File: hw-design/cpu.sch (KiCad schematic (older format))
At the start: 15 parts, among them P1 CONN_02X05, P2 CONN_02X05, U4 LPC1113FBD48/302, X1 10MHz

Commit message: replacing some cached symbols by kicad-library symbols
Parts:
- X1: symbol CRYSTAL -> Crystal
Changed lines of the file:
@@
 $EndComp
 $Comp
-L CRYSTAL X1
+L Crystal X1
 U 1 1 548B6D9D
 P 2700 4700
@@
 	8750 4850 8650 4850
 Wire Wire Line
-	7950 4850 7950 5250
+	7950 4850 7950 4950
+Wire Wire Line
+	7950 4950 7950 5050
+Wire Wire Line
+	7950 5050 7950 5150
+Wire Wire Line
+	7950 5150 7950 5250
 Connection ~ 7950 5050
 Connection ~ 7950 4950
@@
 	5650 3700 5850 3700
 Wire Wire Line
-	3000 4700 3250 4700
+	2850 4700 3100 4700
+Wire Wire Line
+	3100 4700 3250 4700
 Wire Wire Line
 	3100 4850 3100 4700
 Connection ~ 3100 4700
 Wire Wire Line
-	2250 4500 2250 4850
+	2250 4500 2250 4700
+Wire Wire Line
+	2250 4700 2250 4850
 Wire Wire Line
 	2250 4500 3250 4500
 Wire Wire Line
-	2400 4700 2250 4700
+	2550 4700 2250 4700
 Connection ~ 2250 4700
 Wire Wire Line
 	4350 4950 4350 5050
 Wire Wire Line
-	4350 5050 4550 5050
+	4350 5050 4450 5050
+Wire Wire Line
+	4450 5050 4550 5050
 Wire Wire Line
 	4550 5050 4550 4950
@@
 	2250 5150 2250 5250
 Wire Wire Line
-	2250 5250 3100 5250
+	2250 5250 2700 5250
+Wire Wire Line
+	2700 5250 3100 5250
 Wire Wire Line
 	3100 5250 3100 5150
@@
 	5050 1950 5050 2000
 Wire Wire Line
-	4250 1950 4650 1950
+	4250 1950 4350 1950
+Wire Wire Line
+	4350 1950 4450 1950
+Wire Wire Line
+	4450 1950 4550 1950
+Wire Wire Line
+	4550 1950 4650 1950
 Wire Wire Line
 	4550 2100 4550 1950
@@
 Connection ~ 4350 1950
 Wire Wire Line
-	2650 2350 3250 2350
+	2650 2350 2800 2350
+Wire Wire Line
+	2800 2350 3150 2350
+Wire Wire Line
+	3150 2350 3250 2350
 Wire Wire Line
 	2800 2450 2800 2350
@@
 Connection ~ 3150 2350
 Wire Wire Line
-	5650 2950 6850 2950
-Wire Wire Line
-	5650 3050 6850 3050
-Wire Wire Line
-	7350 3050 7800 3050
-Wire Wire Line
-	7350 2950 7800 2950
-Wire Wire Line
-	7350 3150 7800 3150
-Wire Wire Line
-	5900 3150 6850 3150
+	5650 2950 6600 2950
+Wire Wire Line
+	6600 2950 6850 2950
+Wire Wire Line
+	5650 3050 6550 3050
+Wire Wire Line
+	6550 3050 6850 3050
+Wire Wire Line
+	7350 3050 7650 3050
+Wire Wire Line
+	7650 3050 7800 3050
+Wire Wire Line
+	7350 2950 7600 2950
+Wire Wire Line
+	7600 2950 7800 2950
+Wire Wire Line
+	7350 3150 7700 3150
+Wire Wire Line
+	7700 3150 7800 3150
+Wire Wire Line
+	5900 3150 6500 3150
+Wire Wire Line
+	6500 3150 6850 3150
 Connection ~ 6600 2950
 Connection ~ 6550 3050
@@
 	5900 2850 5900 3150
 Wire Wire Line
-	7350 2750 8500 2750
+	7350 2750 7600 2750
+Wire Wire Line
+	7600 2750 8500 2750
 Wire Wire Line
 	8500 2750 8500 2800
@@
 	6500 2850 6850 2850
 Wire Wire Line
-	6500 2400 6500 2850
+	6500 2400 6500 2500
+Wire Wire Line
+	6500 2500 6500 2850
 Wire Wire Line
 	7350 2850 7700 2850

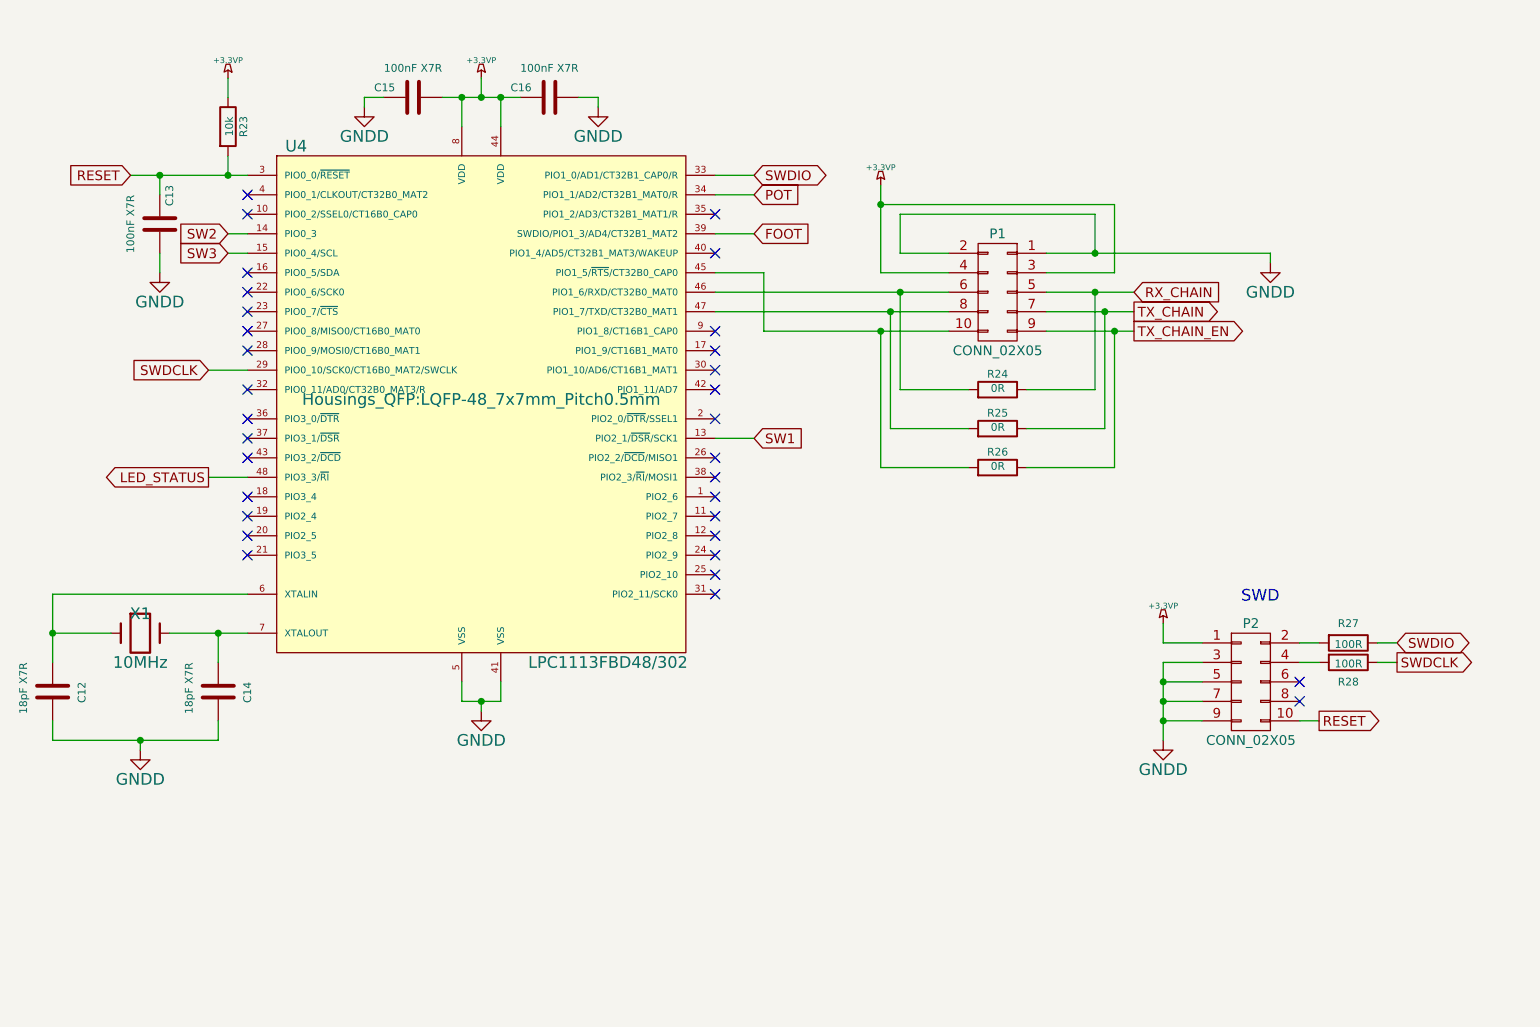
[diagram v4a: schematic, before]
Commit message: sch: updating some cached symbols
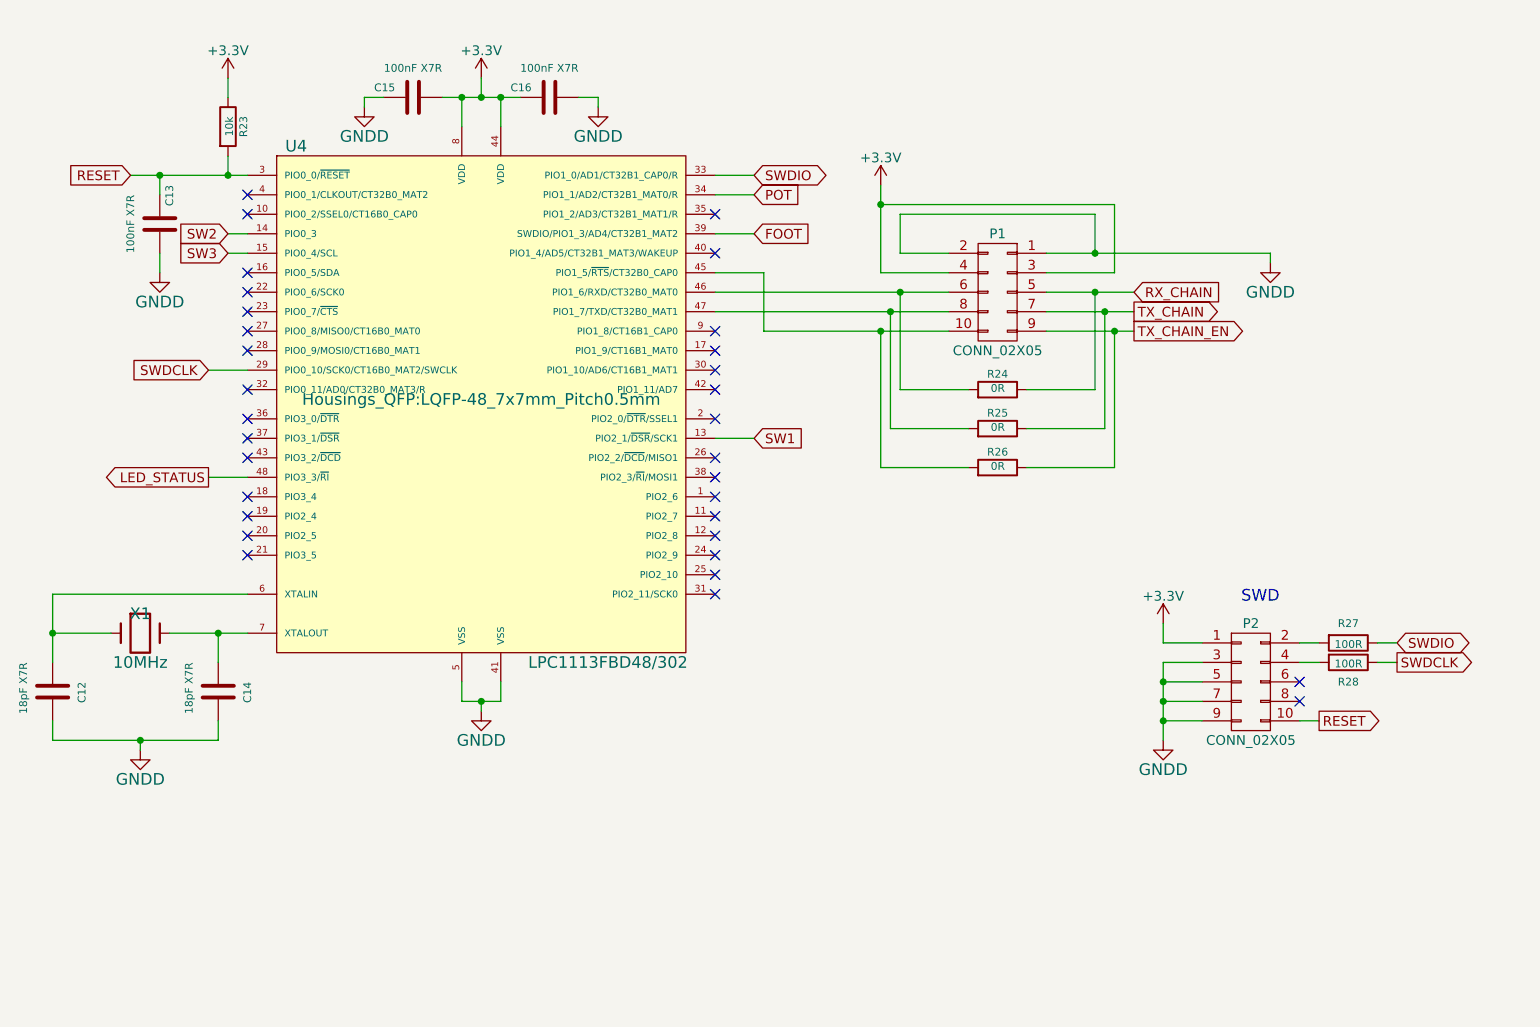
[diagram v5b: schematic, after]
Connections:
- net +3.3VP renamed +3V3
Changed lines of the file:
@@
 LIBS:conn
 LIBS:interface
-LIBS:expression-pedal-cache
 EELAYER 25 0
 EELAYER END
@@
 	1    0    0    -1
 $EndComp
-$Comp
-L +3.3VP #PWR053
-U 1 1 54E3DA42
-P 4450 1850
-F 0 "#PWR053" H 4500 1880 20  0001 C CNN
-F 1 "+3.3VP" H 4450 1940 30  0000 C CNN
-F 2 "" H 4450 1850 60  0000 C CNN
-F 3 "" H 4450 1850 60  0000 C CNN
-	1    4450 1850
-	1    0    0    -1
-$EndComp
 Text GLabel 7800 2950 2    50   Input ~ 0
 RX_CHAIN
@@
 $EndComp
 $Comp
-L +3.3VP #PWR055
-U 1 1 54E51067
-P 6500 2400
-F 0 "#PWR055" H 6550 2430 20  0001 C CNN
-F 1 "+3.3VP" H 6500 2490 30  0000 C CNN
-F 2 "" H 6500 2400 60  0000 C CNN
-F 3 "" H 6500 2400 60  0000 C CNN
-	1    6500 2400
-	1    0    0    -1
-$EndComp
-$Comp
 L GNDD #PWR056
 U 1 1 54E52BA2
@@
 F 3 "" H 2800 2850 60  0000 C CNN
 	1    2800 2850
-	1    0    0    -1
-$EndComp
-$Comp
-L +3.3VP #PWR057
-U 1 1 54E5359B
-P 3150 1850
-F 0 "#PWR057" H 3200 1880 20  0001 C CNN
-F 1 "+3.3VP" H 3150 1940 30  0000 C CNN
-F 2 "" H 3150 1850 60  0000 C CNN
-F 3 "" H 3150 1850 60  0000 C CNN
-	1    3150 1850
 	1    0    0    -1
 $EndComp
@@
 	1    0    0    -1
 $EndComp
-$Comp
-L +3.3VP #PWR059
-U 1 1 54E5E323
-P 7950 4650
-F 0 "#PWR059" H 8000 4680 20  0001 C CNN
-F 1 "+3.3VP" H 7950 4740 30  0000 C CNN
-F 2 "" H 7950 4650 60  0000 C CNN
-F 3 "" H 7950 4650 60  0000 C CNN
-	1    7950 4650
-	1    0    0    -1
-$EndComp
 Wire Wire Line
 	3050 3350 3250 3350
@@
 	8750 4850 8650 4850
 Wire Wire Line
-	7950 4850 7950 4950
-Wire Wire Line
-	7950 4950 7950 5050
-Wire Wire Line
-	7950 5050 7950 5150
-Wire Wire Line
-	7950 5150 7950 5250
+	7950 4850 7950 5250
 Connection ~ 7950 5050
 Connection ~ 7950 4950
@@
 	5650 3700 5850 3700
 Wire Wire Line
-	2850 4700 3100 4700
-Wire Wire Line
-	3100 4700 3250 4700
+	2850 4700 3250 4700
 Wire Wire Line
 	3100 4850 3100 4700
 Connection ~ 3100 4700
 Wire Wire Line
-	2250 4500 2250 4700
-Wire Wire Line
-	2250 4700 2250 4850
+	2250 4500 2250 4850
 Wire Wire Line
 	2250 4500 3250 4500
@@
 	4350 4950 4350 5050
 Wire Wire Line
-	4350 5050 4450 5050
-Wire Wire Line
-	4450 5050 4550 5050
+	4350 5050 4550 5050
 Wire Wire Line
 	4550 5050 4550 4950
@@
 	2250 5150 2250 5250
 Wire Wire Line
-	2250 5250 2700 5250
-Wire Wire Line
-	2700 5250 3100 5250
+	2250 5250 3100 5250
 Wire Wire Line
 	3100 5250 3100 5150
@@
 	5050 1950 5050 2000
 Wire Wire Line
-	4250 1950 4350 1950
-Wire Wire Line
-	4350 1950 4450 1950
-Wire Wire Line
-	4450 1950 4550 1950
-Wire Wire Line
-	4550 1950 4650 1950
+	4250 1950 4650 1950
 Wire Wire Line
 	4550 2100 4550 1950
@@
 Connection ~ 4350 1950
 Wire Wire Line
-	2650 2350 2800 2350
-Wire Wire Line
-	2800 2350 3150 2350
-Wire Wire Line
-	3150 2350 3250 2350
+	2650 2350 3250 2350
 Wire Wire Line
 	2800 2450 2800 2350
@@
 Connection ~ 3150 2350
 Wire Wire Line
-	5650 2950 6600 2950
-Wire Wire Line
-	6600 2950 6850 2950
-Wire Wire Line
-	5650 3050 6550 3050
-Wire Wire Line
-	6550 3050 6850 3050
-Wire Wire Line
-	7350 3050 7650 3050
-Wire Wire Line
-	7650 3050 7800 3050
-Wire Wire Line
-	7350 2950 7600 2950
-Wire Wire Line
-	7600 2950 7800 2950
-Wire Wire Line
-	7350 3150 7700 3150
-Wire Wire Line
-	7700 3150 7800 3150
-Wire Wire Line
-	5900 3150 6500 3150
-Wire Wire Line
-	6500 3150 6850 3150
+	5650 2950 6850 2950
+Wire Wire Line
+	5650 3050 6850 3050
+Wire Wire Line
+	7350 3050 7800 3050
+Wire Wire Line
+	7350 2950 7800 2950
+Wire Wire Line
+	7350 3150 7800 3150
+Wire Wire Line
+	5900 3150 6850 3150
 Connection ~ 6600 2950
 Connection ~ 6550 3050
@@
 	5900 2850 5900 3150
 Wire Wire Line
-	7350 2750 7600 2750
-Wire Wire Line
-	7600 2750 8500 2750
+	7350 2750 8500 2750
 Wire Wire Line
 	8500 2750 8500 2800
@@
 	6500 2850 6850 2850
 Wire Wire Line
-	6500 2400 6500 2500
-Wire Wire Line
-	6500 2500 6500 2850
+	6500 2400 6500 2850
 Wire Wire Line
 	7350 2850 7700 2850
@@
 	1    0    0    -1
 $EndComp
+$Comp
+L +3.3V #PWR?
+U 1 1 556F2DB4
+P 3150 1850
+F 0 "#PWR?" H 3150 1700 50  0001 C CNN
+F 1 "+3.3V" H 3150 1990 50  0000 C CNN
+F 2 "" H 3150 1850 60  0000 C CNN
+F 3 "" H 3150 1850 60  0000 C CNN
+	1    3150 1850
+	1    0    0    -1
+$EndComp
+$Comp
+L +3.3V #PWR?
+U 1 1 556F30B2
+P 7950 4650
+F 0 "#PWR?" H 7950 4500 50  0001 C CNN
+F 1 "+3.3V" H 7950 4790 50  0000 C CNN
+F 2 "" H 7950 4650 60  0000 C CNN
+F 3 "" H 7950 4650 60  0000 C CNN
+	1    7950 4650
+	1    0    0    -1
+$EndComp
+$Comp
+L +3.3V #PWR?
+U 1 1 556F3546
+P 6500 2400
+F 0 "#PWR?" H 6500 2250 50  0001 C CNN
+F 1 "+3.3V" H 6500 2540 50  0000 C CNN
+F 2 "" H 6500 2400 60  0000 C CNN
+F 3 "" H 6500 2400 60  0000 C CNN
+	1    6500 2400
+	1    0    0    -1
+$EndComp
+$Comp
+L +3.3V #PWR?
+U 1 1 556F3767
+P 4450 1850
+F 0 "#PWR?" H 4450 1700 50  0001 C CNN
+F 1 "+3.3V" H 4450 1990 50  0000 C CNN
+F 2 "" H 4450 1850 60  0000 C CNN
+F 3 "" H 4450 1850 60  0000 C CNN
+	1    4450 1850
+	1    0    0    -1
+$EndComp
